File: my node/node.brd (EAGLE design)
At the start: 54.6 x 17.8 mm, 23 parts, among them IC1 , J1 RF24, J4 FTDI, J5 I2C, J6 , J7 , J8 SPI, J9 I2C, U1 W25X40CL, U2 ATMEGA328P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

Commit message: Second version
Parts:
- removed IC1: (no value), v-reg:SOT23
- removed U3: ATSHA204-TSU, SparkFun-IC-Special-Function:SOT23-3
- added 662K: (no value), v-reg:SOT23
- added ATSHA: ATSHA204-TSU, SparkFun-IC-Special-Function:SOT23-3
- added C7: 100nF, SparkFun-Capacitors:0805
- C1: value 100nF -> 10uF; device SparkFun-Capacitors:1206 -> SparkFun-Capacitors:0805
- C2, C6: device SparkFun-Capacitors:1206 -> SparkFun-Capacitors:0805
- moved C3 1.27 mm to (45.7, 21.6)
- moved C4 1.27 mm to (45.7, 24.1)
- moved C5 1.27 mm to (83.8, 27.9)
- moved R1 1.27 mm to (41.9, 22.9), turned to 0 degrees
- turned C2 to 0 degrees
- renumbered U1 to FLASH
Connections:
- net A3: now also ATSHA.1; no longer U3.1
- net GND: now also 662K.1, ATSHA.3, C7.1; no longer IC1.1, U3.3
- net RXI: now also J4.3; no longer J4.2
- net TXO: now also J4.2; no longer J4.3
- net VCC: now also 662K.2, ATSHA.2, C7.2; no longer IC1.2, U3.2
- net VIN: now also 662K.3; no longer IC1.3
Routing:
- net VCC: track 140.7 -> 104.3 mm, vias 1 -> 0
- net MOSI: track 57.3 -> 39.6 mm, vias 0 -> 1
- net MISO: track 36.5 -> 54.3 mm, vias 0 -> 3
- net VIN: track 45.1 -> 28.5 mm, vias 1 -> 0
- net FLASH_CE: track 20.7 -> 35.9 mm, vias 2 -> 4
- net D2: track 51.5 -> 38.3 mm
- net SCK: track 46.3 -> 34.0 mm, vias 0 -> 3
- net RF24_CE: track 27.4 -> 39.1 mm
- net GND: track 147.0 -> 138.0 mm, vias 1 -> 0
- net RXI: track 13.8 -> 22.6 mm
- net RESET: track 66.5 -> 71.8 mm, vias 0 -> 5
- net SCL: track 81.6 -> 86.8 mm, vias 2 -> 4
- net A2: track 11.2 -> 15.2 mm
- net CSN: track 29.6 -> 32.7 mm, vias 1 -> 0
- net TXO: track 16.7 -> 19.7 mm
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- added copper zone on layer 1, net GND
- added copper zone on layer 16, net GND
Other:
- board text added: "TX RX RST GND D2 D3 D4 D5 D6 D7 D8 D9"
- board text removed: "TXO RXI RST GND D2 D3 D4 D5 D6 D7 D8 D9"

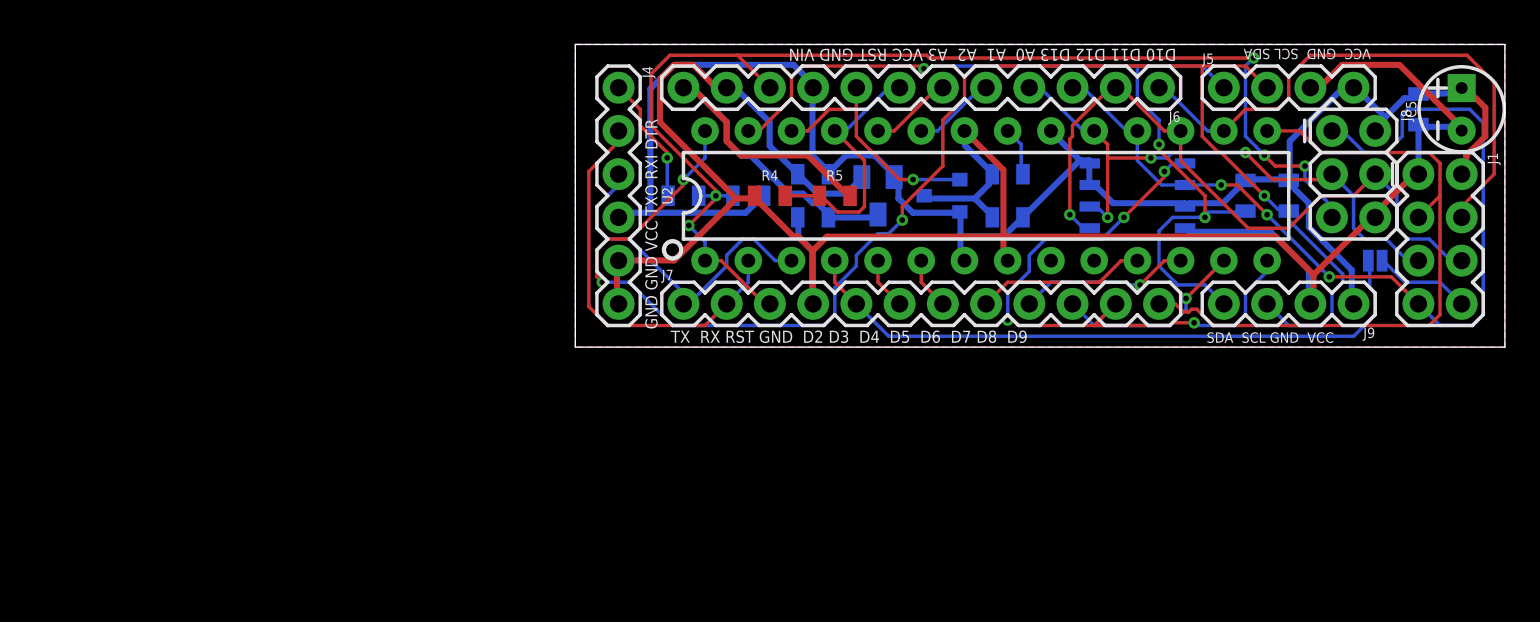
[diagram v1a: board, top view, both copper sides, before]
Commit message: Third version
Fixed FTDI connectior
Pro Mini comatible pinout
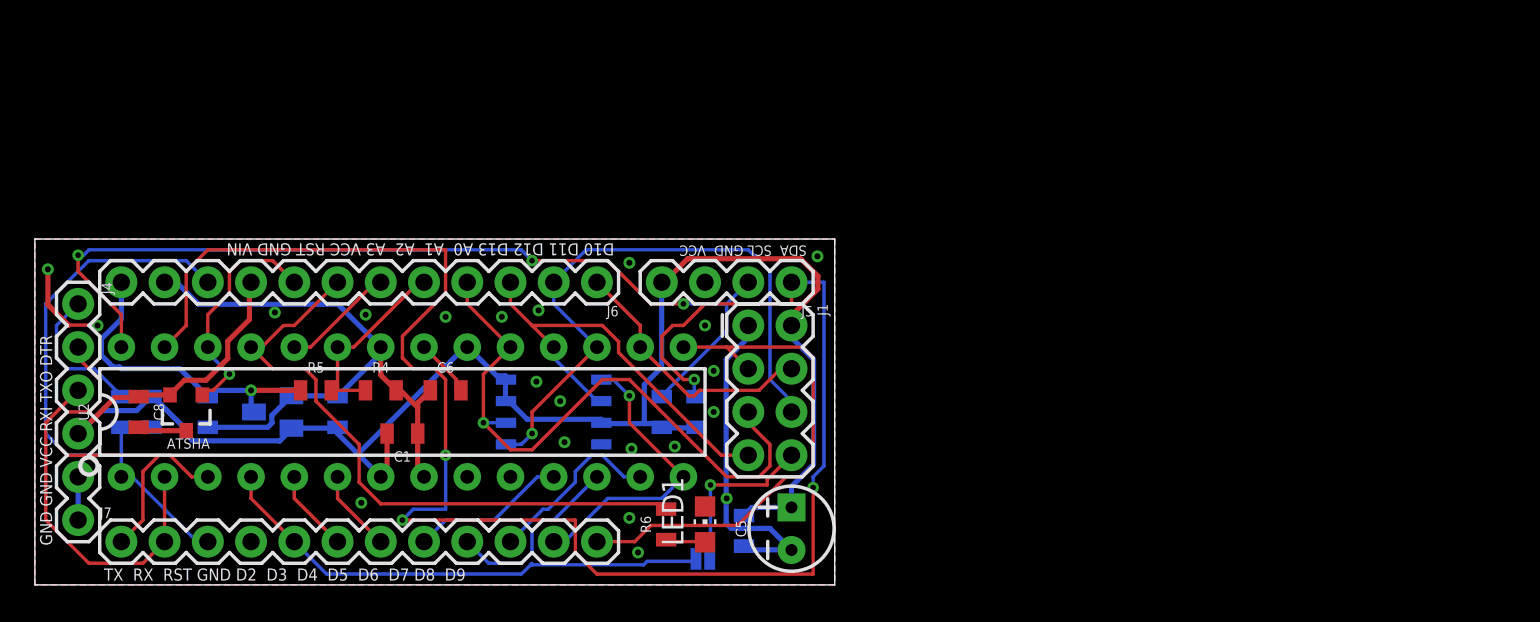
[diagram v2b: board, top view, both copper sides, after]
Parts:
- removed J8: SPI, SparkFun-Connectors:2X3
- removed J9: I2C, SparkFun-Connectors:1X04
- added C8: 100nF, SparkFun-Capacitors:0805
- added LED1: LED, led:CHIP-LED0805
- added R6: 100Ohm, SparkFun-Resistors:0805
- 662K: value (none) -> 662k
- ATSHA: value ATSHA204-TSU -> ATSHA
- C1: value 10uF -> 100nF
- FLASH: value W25X40CL -> SPI FLASH
- J4: value FTDI -> (none)
- J5: value I2C -> (none)
- R2, R3: value 10KOmh -> 10kOmh
- R4: value (none) -> 220k
- R5: value (none) -> 1MOhm
- moved C7 46.7 mm to (41.7, 3.17)
- moved C5 46.4 mm to (44.5, 3.30)
- moved ATSHA 46.2 mm to (8.89, 10.2), flipped to the top, turned to 180 degrees
- moved JP1 43.2 mm to (39.2, 1.52)
- moved J1 40.4 mm to (43.2, 11.4)
- moved R3 39.0 mm to (36.8, 10.2), turned to 270 degrees
- moved 662K 37.8 mm to (14.0, 10.2), turned to 270 degrees
- moved C1 37.8 mm to (21.6, 8.89), flipped to the top
- moved C3 37.4 mm to (10.2, 10.2), turned to 270 degrees
- moved R1 37.3 mm to (6.86, 10.2), turned to 270 degrees
- moved U2 36.6 mm to (21.6, 10.2)
- moved FLASH 36.6 mm to (30.5, 10.2)
- moved J7 35.9 mm to (5.08, 2.54)
- moved C2 35.4 mm to (5.08, 10.2), turned to 90 degrees
- moved C6 35.4 mm to (24.1, 11.4), flipped to the top, turned to 180 degrees
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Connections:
- new net N$3: LED1.A, R6.1
- net A0: now also R4.2, R5.1
- net A2: now also R6.2; no longer R4.2, R5.1
- net GND: now also C8.2, LED1.C; no longer J8.6, J9.2
- net MISO: no longer J8.1
- net MOSI: no longer J8.4
- net RESET: no longer J8.5
- net SCK: no longer J8.3
- net SCL: no longer J9.3
- net SDA: no longer J9.4
- net VCC: now also C8.1; no longer J8.2, J9.1
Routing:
- net GND: track 138.0 -> 71.6 mm, vias 0 -> 21
- net SDA: track 54.1 -> 101.9 mm, vias 3 -> 4
- net RESET: track 71.8 -> 35.7 mm, vias 5 -> 0
- net SCL: track 86.8 -> 54.8 mm, vias 4 -> 3
- net MISO: track 54.3 -> 25.6 mm, vias 3 -> 0
- net A2: track 15.2 -> 36.9 mm
- net FLASH_CE: track 35.9 -> 17.3 mm, vias 4 -> 1
- net CSN: track 32.7 -> 15.6 mm
- net VIN: track 28.5 -> 19.0 mm, vias 0 -> 1
- net RF24_CE: track 39.1 -> 30.6 mm
- net D2: track 38.3 -> 30.1 mm
- net A0: track 4.86 -> 11.2 mm
- net IRQ: track 5.73 -> 10.0 mm, vias 0 -> 1
- net TXO: track 19.7 -> 23.7 mm
- net MOSI: track 39.6 -> 36.1 mm
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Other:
- board size 54.6 x 17.8 mm -> 47 x 20.3 mm
- board text added: "GND GND VCC RXI TXO DTR"
- board text removed: "GND GND VCC TXO RXI DTR"
- board text removed: "VCC GND SCL SDA"
